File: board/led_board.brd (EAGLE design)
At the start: 20.6 x 29.3 mm, 18 parts

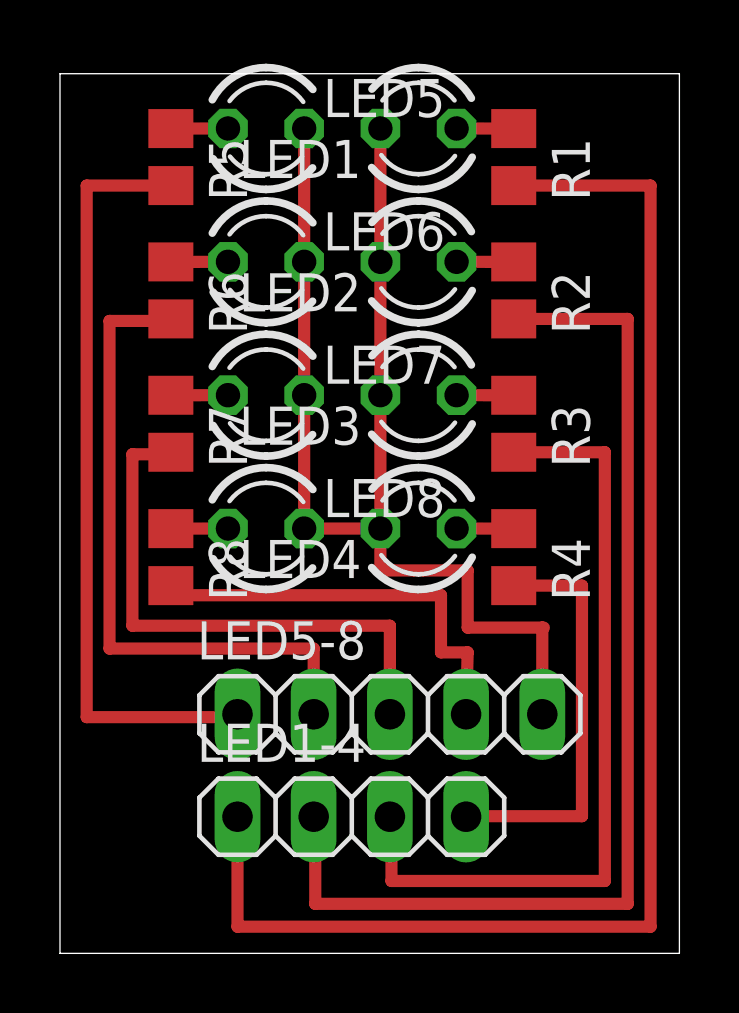
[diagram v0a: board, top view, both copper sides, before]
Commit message: tweaked board layout, defined pins in led.c accordingly
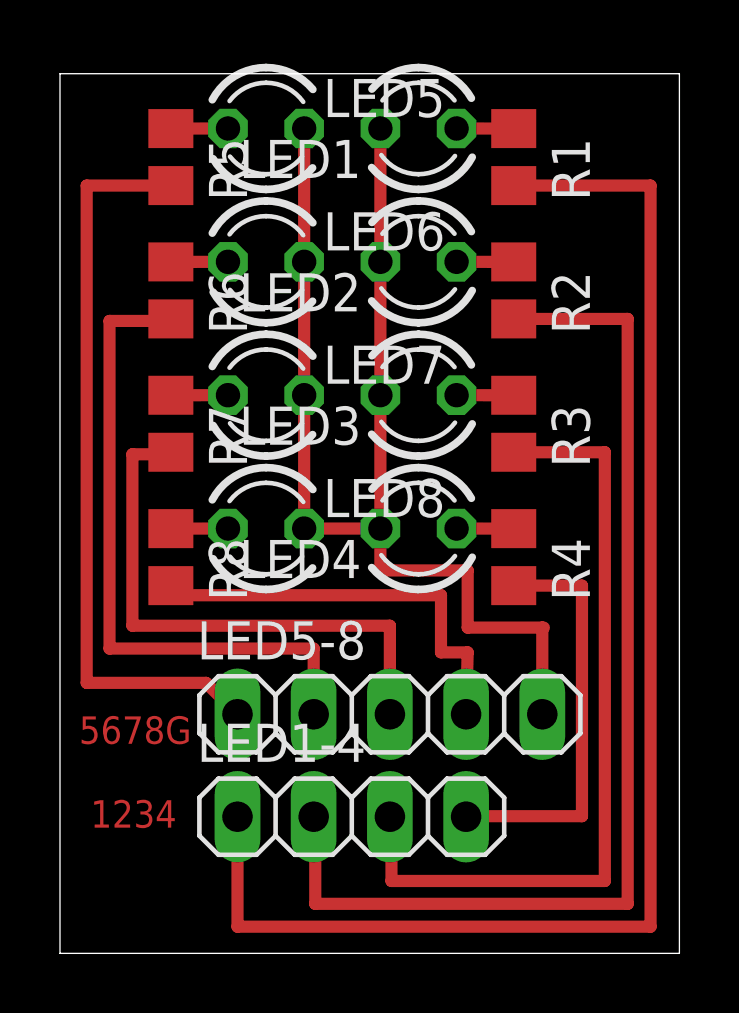
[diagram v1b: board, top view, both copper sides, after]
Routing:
- net LED5: track 25.6 -> 24.8 mm
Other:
- board text added: "1234"
- board text added: "5678G"
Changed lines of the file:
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@@
 <setting verticaltext="up"/>
 </settings>
-<grid distance="5" unitdist="mil" unit="mm" style="lines" multiple="1" display="no" altdistance="5" altunitdist="mil" altunit="mil"/>
+<grid distance="5" unitdist="mil" unit="mil" style="lines" multiple="1" display="no" altdistance="5" altunitdist="mil" altunit="mil"/>
 <layers>
 <layer number="1" name="Top" color="4" fill="1" visible="yes" active="yes"/>
@@
 <wire x1="20.647" y1="29.322" x2="0" y2="29.322" width="0" layer="20"/>
 <wire x1="0" y1="29.322" x2="0" y2="0" width="0" layer="20"/>
+<text x="0.635" y="6.985" size="0.9144" layer="1" font="vector" ratio="28">5678G</text>
+<text x="1.016" y="4.191" size="0.9144" layer="1" font="vector" ratio="28">1234</text>
 </plain>
 <attributes>
@@
 <contactref element="LED5-8" pad="1"/>
 <wire x1="3.694" y1="25.5935" x2="0.889" y2="25.5935" width="0.4064" layer="1"/>
-<wire x1="0.889" y1="25.5935" x2="0.889" y2="7.874" width="0.4064" layer="1"/>
-<wire x1="0.889" y1="7.874" x2="5.9165" y2="7.874" width="0.4064" layer="1"/>
-<wire x1="5.9165" y1="7.874" x2="5.9165" y2="7.9705" width="0.4064" layer="1"/>
+<wire x1="0.889" y1="25.5935" x2="0.889" y2="9.017" width="0.4064" layer="1"/>
+<wire x1="5.9165" y1="7.9705" x2="4.87" y2="9.017" width="0.4064" layer="1"/>
+<wire x1="4.87" y1="9.017" x2="0.889" y2="9.017" width="0.4064" layer="1"/>
 </signal>
 <signal name="LED6">

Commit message: added values to resistors on led board
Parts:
- R1, R2, R3, R4, R5, R6, R7, R8: value (none) -> 470
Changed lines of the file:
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@@
 <element name="LED7" library="led" package="LED3MM" value="" x="6.869" y="18.606"/>
 <element name="LED8" library="led" package="LED3MM" value="" x="6.869" y="14.161"/>
-<element name="R1" library="resistor" package="R0805" value="" x="15.124" y="26.5435" rot="R270"/>
-<element name="R2" library="resistor" package="R0805" value="" x="15.124" y="22.0985" rot="R270"/>
-<element name="R3" library="resistor" package="R0805" value="" x="15.124" y="17.6535" rot="R270"/>
-<element name="R4" library="resistor" package="R0805" value="" x="15.124" y="13.2085" rot="R270"/>
-<element name="R5" library="resistor" package="R0805" value="" x="3.694" y="26.5435" rot="R270"/>
-<element name="R6" library="resistor" package="R0805" value="" x="3.694" y="22.0985" rot="R270"/>
-<element name="R7" library="resistor" package="R0805" value="" x="3.694" y="17.6535" rot="R270"/>
-<element name="R8" library="resistor" package="R0805" value="" x="3.694" y="13.2085" rot="R270"/>
+<element name="R1" library="resistor" package="R0805" value="470" x="15.124" y="26.5435" rot="R270"/>
+<element name="R2" library="resistor" package="R0805" value="470" x="15.124" y="22.0985" rot="R270"/>
+<element name="R3" library="resistor" package="R0805" value="470" x="15.124" y="17.6535" rot="R270"/>
+<element name="R4" library="resistor" package="R0805" value="470" x="15.124" y="13.2085" rot="R270"/>
+<element name="R5" library="resistor" package="R0805" value="470" x="3.694" y="26.5435" rot="R270"/>
+<element name="R6" library="resistor" package="R0805" value="470" x="3.694" y="22.0985" rot="R270"/>
+<element name="R7" library="resistor" package="R0805" value="470" x="3.694" y="17.6535" rot="R270"/>
+<element name="R8" library="resistor" package="R0805" value="470" x="3.694" y="13.2085" rot="R270"/>
 <element name="LED1-4" library="pinhead" package="1X04" value="JP1" x="9.7265" y="4.555"/>
 <element name="LED5-8" library="pinhead" package="1X05" value="JP2" x="10.9965" y="7.9705"/>
